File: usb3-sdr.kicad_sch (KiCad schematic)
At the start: 9 parts, among them J1 BNC IN, Q1 BSS84, U5 TCA6408ARGT, U7 SC18IS606PW

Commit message: Fix SPI voltages, etc
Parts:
- R1: renamed from R36; footprint (none) -> Resistor_SMD:R_0603_1608Metric
- R2: renamed from R35; footprint (none) -> Resistor_SMD:R_0603_1608Metric
- R3: renamed from R34; footprint (none) -> Resistor_SMD:R_0603_1608Metric
- renumbered R1 to R4, U5 to U1, U7 to U2
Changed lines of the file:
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@@
-	(wire
-		(pts
-			(xy 139.7 62.23) (xy 149.86 62.23)
-		)
-		(stroke
-			(width 0)
-			(type default)
-		)
-	)
 	(wire
 		(pts
@@
 	(wire
 		(pts
-			(xy 139.7 64.77) (xy 149.86 64.77)
-		)
-		(stroke
-			(width 0)
-			(type default)
-		)
-	)
-	(wire
-		(pts
 			(xy 163.83 50.8) (xy 172.72 50.8)
 		)
@@
 	(wire
 		(pts
-			(xy 139.7 67.31) (xy 149.86 67.31)
-		)
-		(stroke
-			(width 0)
-			(type default)
-		)
-	)
-	(wire
-		(pts
 			(xy 40.64 53.34) (xy 40.64 59.69)
 		)
@@
 		(pts
 			(xy 187.96 64.77) (xy 198.12 64.77)
-		)
-		(stroke
-			(width 0)
-			(type default)
-		)
-	)
-	(wire
-		(pts
-			(xy 139.7 59.69) (xy 149.86 59.69)
 		)
 		(stroke
@@
 	)
 	(label "SCLK"
-		(at 139.7 62.23 0)
+		(at 139.7 62.23 180)
 		(effects
 			(font
 				(size 1.27 1.27)
 			)
-			(justify left bottom)
+			(justify right bottom)
 		)
 	)
@@
 	)
 	(label "PGA_~{CS}"
-		(at 139.7 59.69 0)
+		(at 139.7 59.69 180)
 		(effects
 			(font
 				(size 1.27 1.27)
 			)
-			(justify left bottom)
+			(justify right bottom)
 		)
 	)
@@
 		(dnp no)
 		(fields_autoplaced yes)
-		(property "Reference" "#PWR0135"
+		(property "Reference" "#PWR02"
 			(at 40.64 57.15 0)
 			(effects
@@
 			(project ""
 				(path "/c130ee0c-52ab-4414-8ea8-abd1a940c0be"
-					(reference "#PWR0135")
+					(reference "#PWR02")
 					(unit 1)
 				)
@@
 		(dnp no)
 		(fields_autoplaced yes)
-		(property "Reference" "#PWR0125"
+		(property "Reference" "#PWR08"
 			(at 66.04 39.37 0)
 			(effects
@@
 			(project "usb3-sdr"
 				(path "/c130ee0c-52ab-4414-8ea8-abd1a940c0be"
-					(reference "#PWR0125")
+					(reference "#PWR08")
 					(unit 1)
 				)
@@
 		(dnp no)
 		(fields_autoplaced yes)
-		(property "Reference" "#PWR0139"
+		(property "Reference" "#PWR05"
 			(at 50.8 127 0)
 			(effects
@@
 			(project ""
 				(path "/c130ee0c-52ab-4414-8ea8-abd1a940c0be"
-					(reference "#PWR0139")
+					(reference "#PWR05")
 					(unit 1)
 				)
@@
 		(dnp no)
 		(fields_autoplaced yes)
-		(property "Reference" "R1"
+		(property "Reference" "R4"
 			(at 231.14 111.7599 0)
 			(effects
@@
 			(project ""
 				(path "/c130ee0c-52ab-4414-8ea8-abd1a940c0be"
-					(reference "R1")
+					(reference "R4")
 					(unit 1)
 				)
@@
 		(dnp no)
 		(fields_autoplaced yes)
-		(property "Reference" "R35"
+		(property "Reference" "R2"
 			(at 154.94 105.4099 0)
 			(effects
@@
 			)
 		)
-		(property "Footprint" ""
+		(property "Footprint" "Resistor_SMD:R_0603_1608Metric"
 			(at 150.622 106.68 90)
 			(effects
@@
 			(project "usb3-sdr"
 				(path "/c130ee0c-52ab-4414-8ea8-abd1a940c0be"
-					(reference "R35")
+					(reference "R2")
 					(unit 1)
 				)
@@
 		(dnp no)
 		(fields_autoplaced yes)
-		(property "Reference" "#PWR0137"
+		(property "Reference" "#PWR010"
 			(at 66.04 129.54 0)
 			(effects
@@
 			(project ""
 				(path "/c130ee0c-52ab-4414-8ea8-abd1a940c0be"
-					(reference "#PWR0137")
+					(reference "#PWR010")
 					(unit 1)
 				)
@@
 		(dnp no)
 		(fields_autoplaced yes)
-		(property "Reference" "#PWR0138"
+		(property "Reference" "#PWR07"
 			(at 63.5 93.98 0)
 			(effects
@@
 			(project ""
 				(path "/c130ee0c-52ab-4414-8ea8-abd1a940c0be"
-					(reference "#PWR0138")
+					(reference "#PWR07")
 					(unit 1)
 				)
@@
 		(dnp no)
 		(fields_autoplaced yes)
-		(property "Reference" "#PWR02"
+		(property "Reference" "#PWR014"
 			(at 228.6 113.03 0)
 			(effects
@@
 			(project "usb3-sdr"
 				(path "/c130ee0c-52ab-4414-8ea8-abd1a940c0be"
-					(reference "#PWR02")
+					(reference "#PWR014")
 					(unit 1)
 				)
@@
 		(dnp no)
 		(fields_autoplaced yes)
-		(property "Reference" "#PWR0129"
+		(property "Reference" "#PWR013"
 			(at 162.56 106.68 0)
 			(effects
@@
 			(project ""
 				(path "/c130ee0c-52ab-4414-8ea8-abd1a940c0be"
-					(reference "#PWR0129")
+					(reference "#PWR013")
 					(unit 1)
 				)
@@
 		(dnp no)
 		(fields_autoplaced yes)
-		(property "Reference" "R34"
+		(property "Reference" "R3"
 			(at 165.1 105.4099 0)
 			(effects
@@
 			)
 		)
-		(property "Footprint" ""
+		(property "Footprint" "Resistor_SMD:R_0603_1608Metric"
 			(at 160.782 106.68 90)
 			(effects
@@
 			(project ""
 				(path "/c130ee0c-52ab-4414-8ea8-abd1a940c0be"
-					(reference "R34")
+					(reference "R3")
 					(unit 1)
 				)
@@
 		(dnp no)
 		(fields_autoplaced yes)
-		(property "Reference" "#PWR051"
+		(property "Reference" "#PWR09"
 			(at 66.04 78.74 0)
 			(effects
@@
 			(project "usb3-sdr"
 				(path "/c130ee0c-52ab-4414-8ea8-abd1a940c0be"
-					(reference "#PWR051")
+					(reference "#PWR09")
 					(unit 1)
 				)
@@
 		(dnp no)
 		(fields_autoplaced yes)
-		(property "Reference" "U5"
+		(property "Reference" "U1"
 			(at 68.1833 39.37 0)
 			(effects
@@
 			(project "usb3-sdr"
 				(path "/c130ee0c-52ab-4414-8ea8-abd1a940c0be"
-					(reference "U5")
+					(reference "U1")
 					(unit 1)
 				)
@@
 		(dnp no)
 		(fields_autoplaced yes)
-		(property "Reference" "#PWR01"
+		(property "Reference" "#PWR011"
 			(at 132.08 88.9 0)
 			(effects
@@
 			(project "usb3-sdr"
 				(path "/c130ee0c-52ab-4414-8ea8-abd1a940c0be"
-					(reference "#PWR01")
+					(reference "#PWR011")
 					(unit 1)
 				)
@@
 		(dnp no)
 		(fields_autoplaced yes)
-		(property "Reference" "#PWR057"
+		(property "Reference" "#PWR06"
 			(at 63.5 45.72 0)
 			(effects
@@
 			(project "usb3-sdr"
 				(path "/c130ee0c-52ab-4414-8ea8-abd1a940c0be"
-					(reference "#PWR057")
+					(reference "#PWR06")
 					(unit 1)
 				)
@@
 		(dnp no)
 		(fields_autoplaced yes)
-		(property "Reference" "#PWR0134"
+		(property "Reference" "#PWR012"
 			(at 152.4 106.68 0)
 			(effects
@@
 			(project "usb3-sdr"
 				(path "/c130ee0c-52ab-4414-8ea8-abd1a940c0be"
-					(reference "#PWR0134")
+					(reference "#PWR012")
 					(unit 1)
 				)
@@
 		(dnp no)
 		(fields_autoplaced yes)
-		(property "Reference" "#PWR03"
+		(property "Reference" "#PWR015"
 			(at 233.68 135.89 0)
 			(effects
@@
 			(project ""
 				(path "/c130ee0c-52ab-4414-8ea8-abd1a940c0be"
-					(reference "#PWR03")
+					(reference "#PWR015")
 					(unit 1)
 				)
@@
 		(dnp no)
 		(fields_autoplaced yes)
-		(property "Reference" "U7"
+		(property "Reference" "U2"
 			(at 68.1833 123.19 0)
 			(effects
@@
 			(project ""
 				(path "/c130ee0c-52ab-4414-8ea8-abd1a940c0be"
-					(reference "U7")
+					(reference "U2")
 					(unit 1)
 				)
@@
 		(dnp no)
 		(fields_autoplaced yes)
-		(property "Reference" "#PWR0136"
+		(property "Reference" "#PWR04"
 			(at 50.8 73.66 0)
 			(effects
@@
 			(project ""
 				(path "/c130ee0c-52ab-4414-8ea8-abd1a940c0be"
-					(reference "#PWR0136")
+					(reference "#PWR04")
 					(unit 1)
 				)
@@
 		(dnp no)
 		(fields_autoplaced yes)
-		(property "Reference" "R36"
+		(property "Reference" "R1"
 			(at 31.75 96.5199 0)
 			(effects
@@
 			)
 		)
-		(property "Footprint" ""
+		(property "Footprint" "Resistor_SMD:R_0603_1608Metric"
 			(at 27.432 97.79 90)
 			(effects
@@
 			(project ""
 				(path "/c130ee0c-52ab-4414-8ea8-abd1a940c0be"
-					(reference "R36")
+					(reference "R1")
 					(unit 1)
 				)
@@
 		(dnp no)
 		(fields_autoplaced yes)
-		(property "Reference" "#PWR0140"
+		(property "Reference" "#PWR03"
 			(at 40.64 104.14 0)
 			(effects
@@
 			(project "usb3-sdr"
 				(path "/c130ee0c-52ab-4414-8ea8-abd1a940c0be"
-					(reference "#PWR0140")
+					(reference "#PWR03")
 					(unit 1)
 				)
@@
 		(dnp no)
 		(fields_autoplaced yes)
-		(property "Reference" "#PWR04"
+		(property "Reference" "#PWR01"
 			(at 29.21 97.79 0)
 			(effects
@@
 			(project ""
 				(path "/c130ee0c-52ab-4414-8ea8-abd1a940c0be"
-					(reference "#PWR04")
+					(reference "#PWR01")
 					(unit 1)
 				)

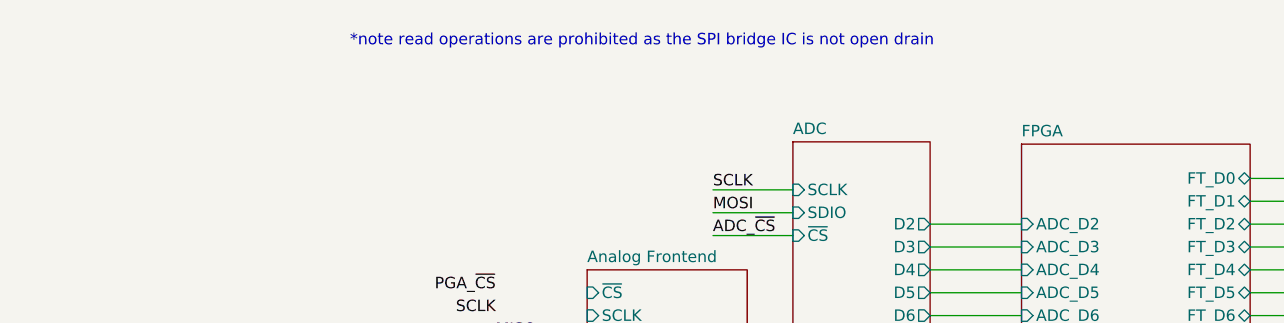
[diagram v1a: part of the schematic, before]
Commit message: Fix typo in note and fix gitignore
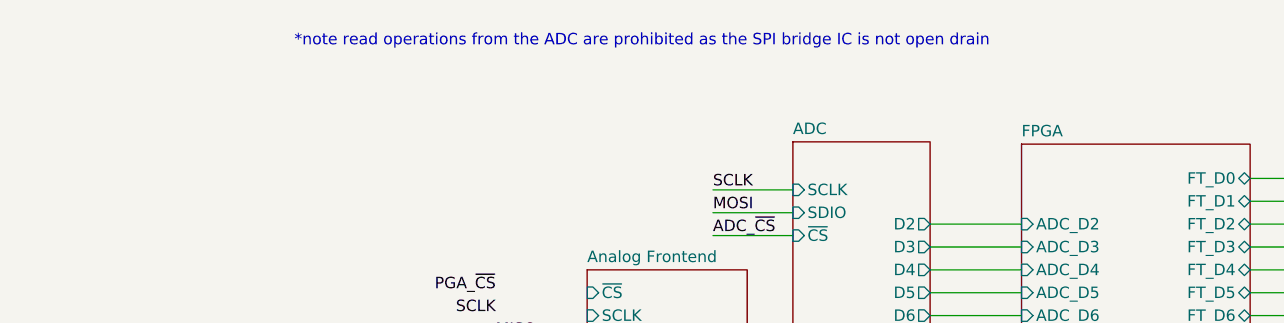
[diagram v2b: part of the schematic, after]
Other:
- note added: "*note read operations from the ADC are prohibited as the SPI bridge IC is not open drain"
- note removed: "*note read operations are prohibited as the SPI bridge IC is not open drain"
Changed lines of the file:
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@@
 		)
 	)
-	(text "*note read operations are prohibited as the SPI bridge IC is not open drain"
+	(text "*note read operations from the ADC are prohibited as the SPI bridge IC is not open drain"
 		(exclude_from_sim no)
 		(at 155.956 31.75 0)
